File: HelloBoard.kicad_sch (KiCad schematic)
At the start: 52 parts, among them J1 USB_B_Micro, J2 Conn_01x04_Pin, J3 Conn_01x04_Pin, J4 Conn_02x08_Top_Bottom, J5 Conn_01x02, SW1 SW_Push, SW2 SW_Push, U1 STM32F103C8T6, U2 AMS1117-3.3, U3 TMP235A2DCKR, U4 ADXL343, Y1 16MHz

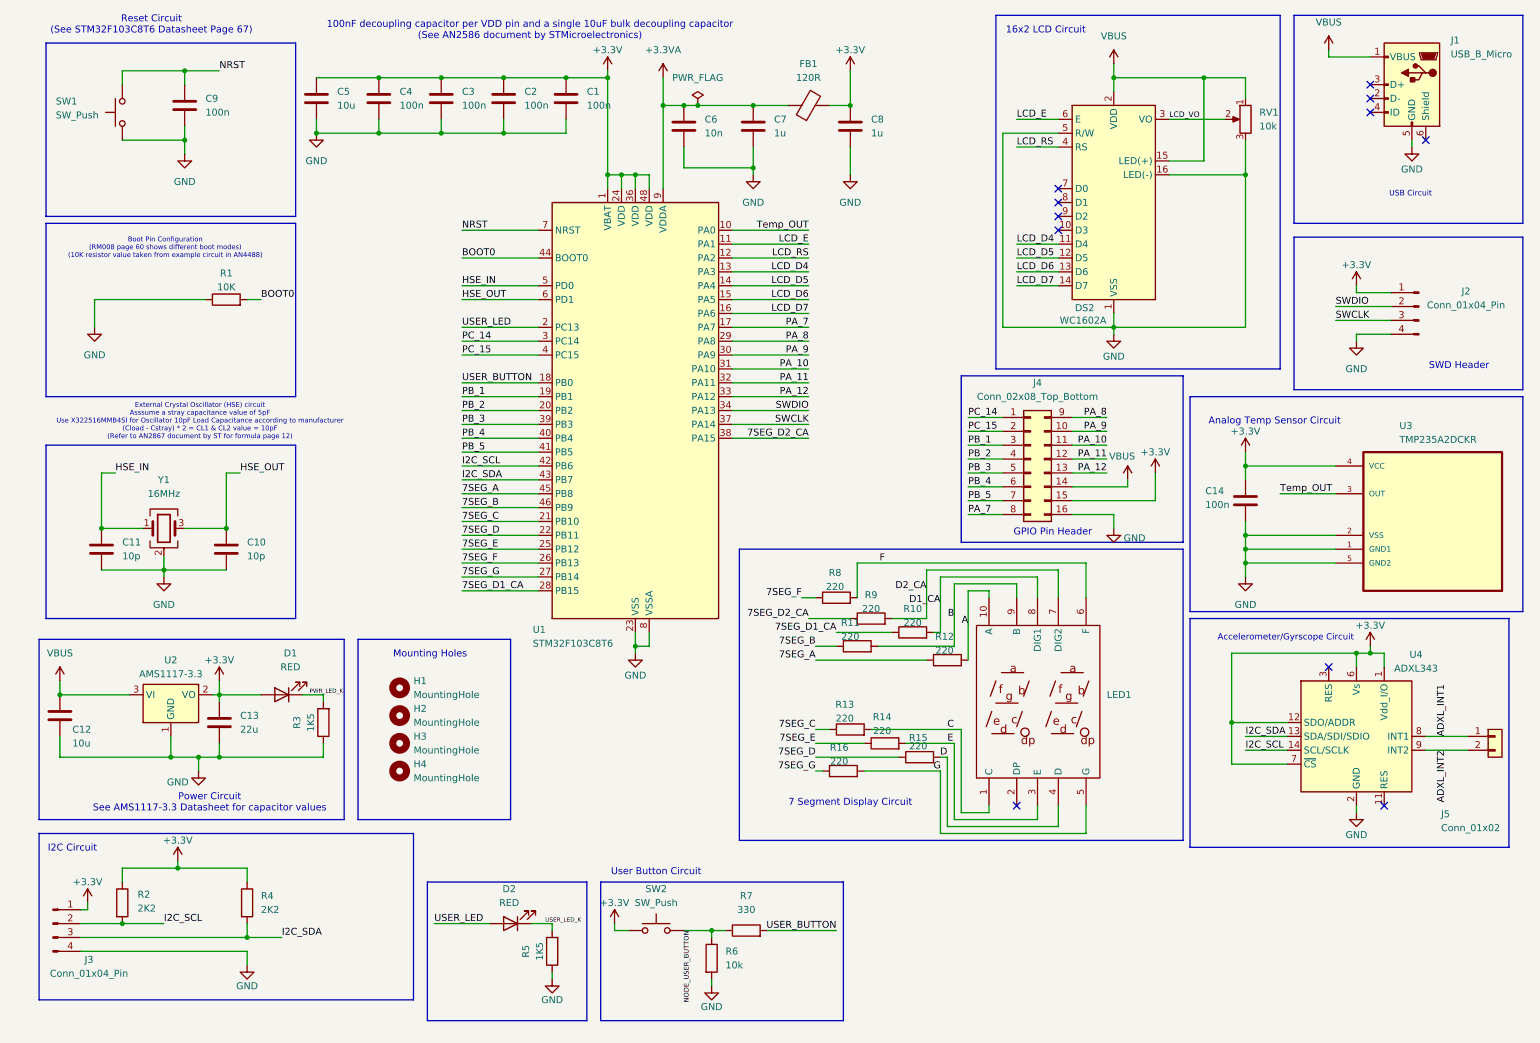
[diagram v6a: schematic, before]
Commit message: TODO 7segment digit control
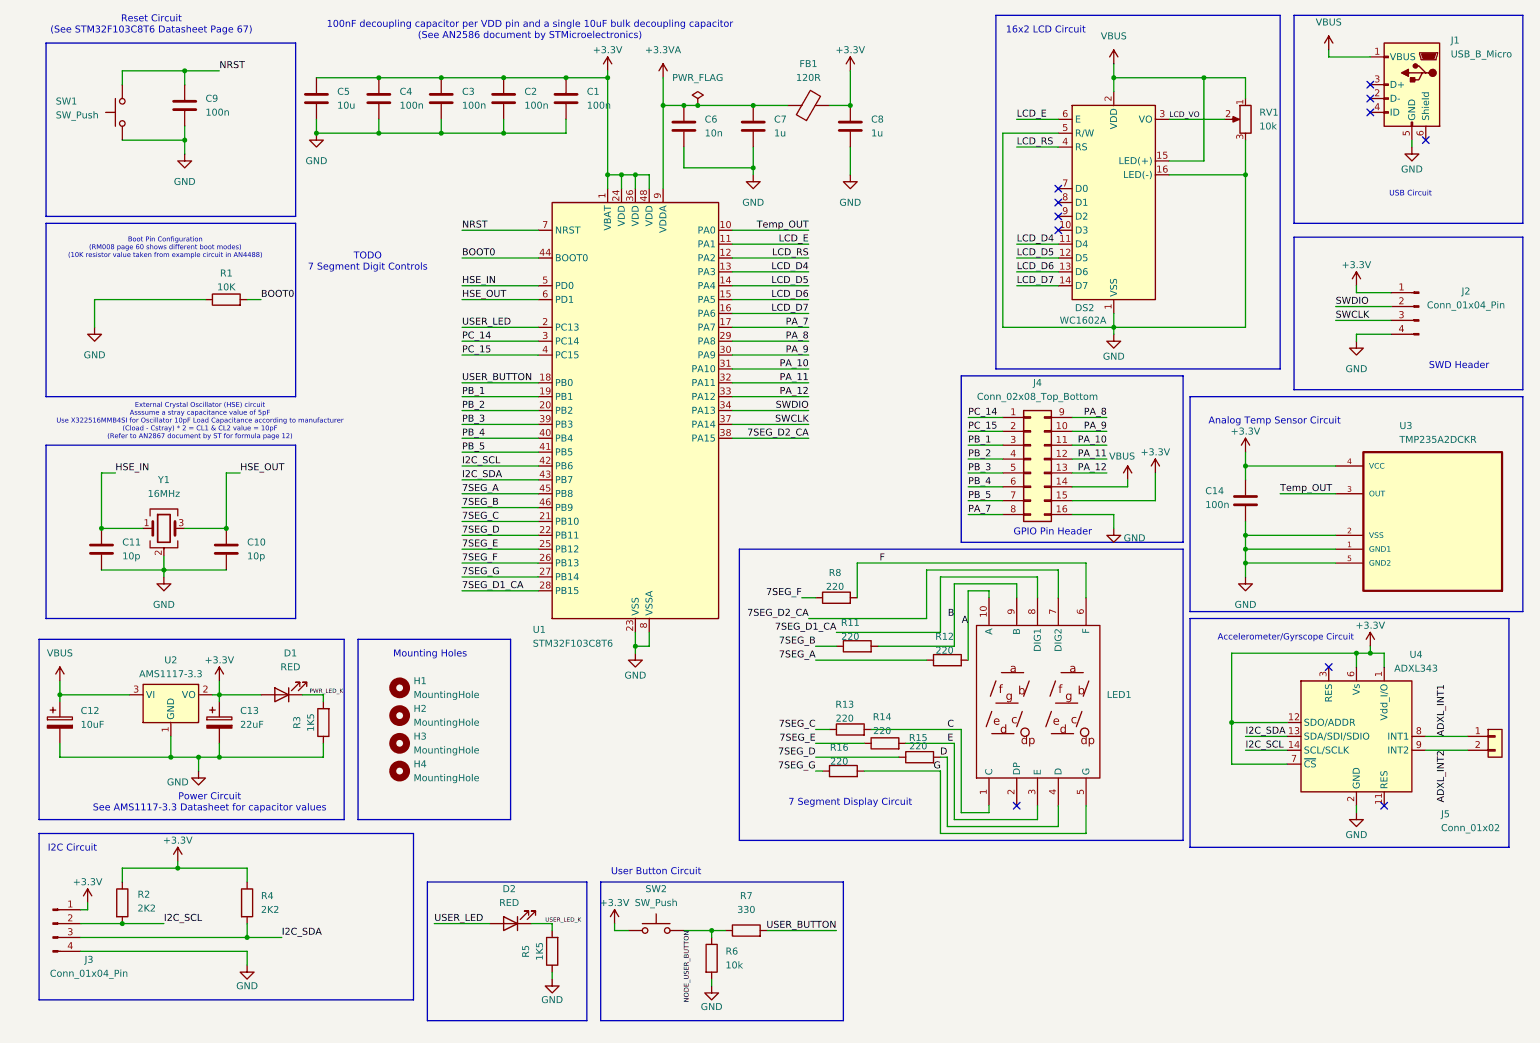
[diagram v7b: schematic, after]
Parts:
- removed C12: 10u, Capacitor_Tantalum_SMD:CP_EIA-3528-21_Kemet-B, symbol Device:C
- removed C13: 22u, Capacitor_Tantalum_SMD:CP_EIA-3528-21_Kemet-B, symbol Device:C
- removed R10, R9: 220, Resistor_SMD:R_0402_1005Metric, symbol Device:R
- added C12: 10uF, Capacitor_Tantalum_SMD:CP_EIA-3528-21_Kemet-B, symbol Device:C_Polarized
- added C13: 22uF, Capacitor_Tantalum_SMD:CP_EIA-3528-21_Kemet-B, symbol Device:C_Polarized
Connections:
- net D1_CA is gone; now on net 7SEG_D1_CA: LED1.8 (DIG1)
- net D2_CA is gone; now on net 7SEG_D2_CA: LED1.7 (DIG2)
- net +3.3V: now also C13.1
- net GND: now also C12.2, C13.2
- net VBUS: now also C12.1
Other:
- note added: "TODO 7 Segment Digit Controls"

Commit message: board finished (for now)
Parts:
- added Q1, Q2: AO3401A, Package_TO_SOT_SMD:SOT-23, symbol Transistor_FET:AO3401A
- added R10, R9: 1K, Resistor_SMD:R_0603_1608Metric, symbol Device:R
- added R17, R18: 10k, Resistor_SMD:R_0603_1608Metric, symbol Device:R
- R3, R5: value 1K5 -> 1K
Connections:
- net +3.3V: now also Q1.2 (S), Q2.2 (S), R17.1, R18.1
- net 7SEG_D1_CA: now also Q1.3 (D); no longer U1.28 (PB15)
- net 7SEG_D2_CA: now also Q2.3 (D); no longer U1.38 (PA15)
- new net D1_CA: R9.2, U1.28 (PB15)
- new net D2_CA: R10.2, U1.38 (PA15)
- new net Gate_Q1: Q1.1 (G), R17.2, R9.1
- new net Gate_Q2: Q2.1 (G), R10.1, R18.2
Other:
- note added: "7 Segment Digit Control"
- note removed: "TODO 7 Segment Digit Controls"
- moved on the sheet: D2, H1, H2, H3, H4, R5, R6, R7, SW2
